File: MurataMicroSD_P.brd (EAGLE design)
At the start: 25.6 x 12.8 mm, 57 parts, among them U1 IC_BLE_LBCA2HNZYZ-711, U2 IC_BLE_LBCA2HNZYZ-711, U3 IC_BLE_LBCA2HNZYZ-711, U4 IC_BLE_LBCA2HNZYZ-711, U5 IC_BLE_LBCA2HNZYZ-711, U6 IC_BLE_LBCA2HNZYZ-711

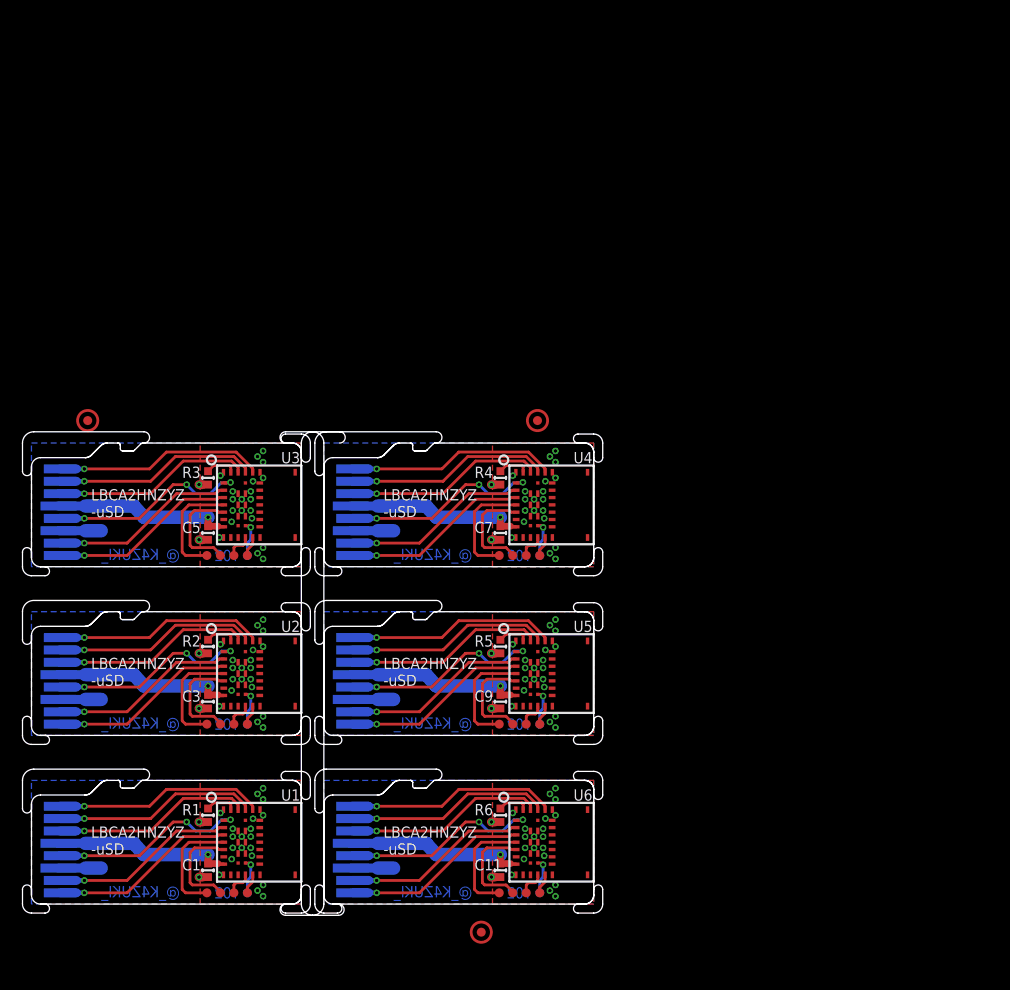
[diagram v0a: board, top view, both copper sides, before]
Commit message: [ uSD ] panelise as r3
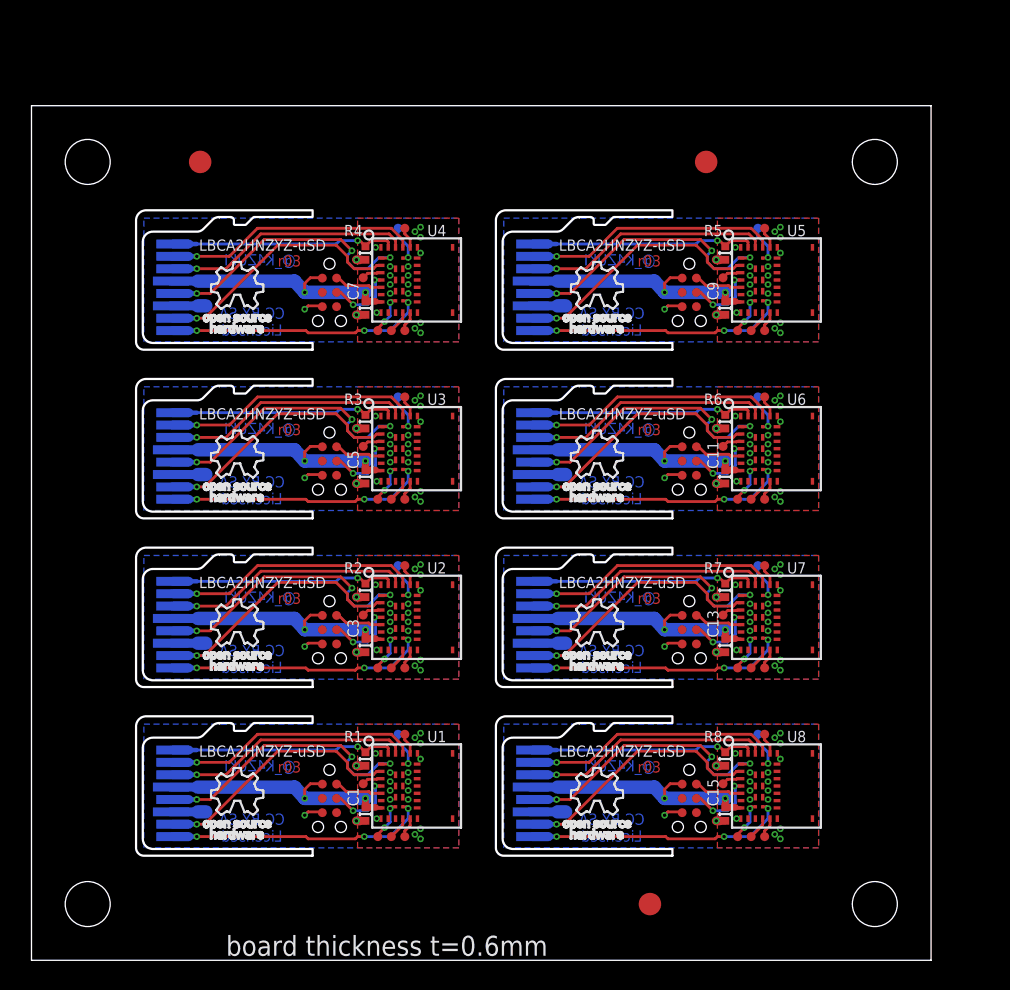
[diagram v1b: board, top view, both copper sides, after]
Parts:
- added C12, C14: BOARD_MICROSD, mylib:BOARD_MICROSD
- added C13, C15, R7, R8: (no value), mylib:C0402
- added CON1, CON2, CON3, CON4, CON5, CON6, CON7, CON8: CON_TC2030-CTL-NL, mylib:CON_TC2030-IDC-NL
- added TP34, TP35, TP36, TP37, TP38, TP39, TP40, TP41, TP42, TP43, TP44, TP45, TP46, TP47, TP48, TP49, TP50, TP51: TPTP08R, testpad_local:TP08R
- added U7, U8: IC_BLE_LBCA2HNZYZ-711, mylib:IC_MURATA_LBCA2HNZYZ-711
- TP3, TP4, TP5: value TPTP08R -> TPTP20R; device testpad_local:TP08R -> testpad_local:TP20R
- moved TP30 63.2 mm to (65.2, 65.1)
- moved TP31 62.2 mm to (64.6, 65.1)
- moved TP33 57.1 mm to (61.5, 60.7)
- moved TP29 55.3 mm to (65.2, 56.0)
- moved TP32 53.4 mm to (62.8, 56.0)
- moved TP25 45.3 mm to (32.6, 65.1), flipped to the bottom
- moved TP24 44.9 mm to (33.2, 65.1)
- moved TP27 42.3 mm to (29.5, 60.7)
- moved C11 40.3 mm to (61.7, 43.0)
- moved C9 40.3 mm to (61.7, 58.0)
- moved R5 40.3 mm to (61.7, 62.9)
- moved R6 40.3 mm to (61.7, 47.9)
- moved U5 40.3 mm to (62.5, 64.0)
- moved U6 40.3 mm to (62.5, 49.0)
- moved TP28 39.7 mm to (64.0, 56.0)
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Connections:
- removed net DAT10: C8.1_DAT2, U5.22
- removed net DAT11: C10.8_DAT1, U6.3
- removed net DAT12: C10.1_DAT2, U6.22
- removed net DAT9: C8.8_DAT1, U5.3
- new net !CS!6: C12.2_CS, U7.23
- new net !CS!7: C14.2_CS, U8.23
- new net 3.3V6: C12.4_VDD, C13.1, CON7.1, U7.7
- new net 3.3V7: C14.4_VDD, C15.1, CON8.1, U8.7
- new net GND6: C12.6_VSS, C13.2, CON7.5, R7.1, U7.15, U7.16, U7.17, U7.18, U7.20, U7.21, U7.26, U7.27, U7.28, U7.29, U7.32, U7.33, U7.34, U7.6, U7.8
- new net GND7: C14.6_VSS, C15.2, CON8.5, R8.1, U8.15, U8.16, U8.17, U8.18, U8.20, U8.21, U8.26, U8.27, U8.28, U8.29, U8.32, U8.33, U8.34, U8.6, U8.8
- new net MISO6: C12.7_MISO, U7.2
- new net MISO7: C14.7_MISO, U8.2
- new net N$13: C12.1_DAT2, R7.2, U7.25
- new net N$14: C12.8_DAT1, U7.31
- new net N$15: C14.1_DAT2, R8.2, U8.25
- new net N$16: C14.8_DAT1, U8.31
- new net P0_13: TP28.TP, U5.11
- new net P0_14: TP29.TP, U5.12
- new net P0_15: TP30.TP, U5.22
- new net P0_16: TP34.TP, U6.11
- new net P0_17: TP35.TP, U6.12
- new net P0_18: TP36.TP, U6.22
- new net P0_19: TP40.TP, U7.11
- new net P0_20: TP41.TP, U7.12
- new net P0_21: TP42.TP, U7.22
- new net P0_22: TP46.TP, U8.11
- new net P0_23: TP47.TP, U8.12
- new net P0_24: TP48.TP, U8.22
- new net P1_0: TP10.TP, U1.35
- new net P1_1: TP11.TP, U1.30
- new net P1_10: TP37.TP, U6.35
- new net P1_11: TP38.TP, U6.30
- new net P1_12: TP43.TP, U7.35
- new net P1_13: TP44.TP, U7.30
- new net P1_14: TP49.TP, U8.35
- new net P1_15: TP50.TP, U8.30
- new net P1_2: TP13.TP, U2.35
- new net P1_3: TP14.TP, U2.30
- new net P1_4: TP19.TP, U3.35
- new net P1_5: TP20.TP, U3.30
- new net P1_6: TP25.TP, U4.35
- new net P1_7: TP26.TP, U4.30
- new net P1_8: TP31.TP, U5.35
- new net P1_9: TP32.TP, U5.30
- new net RXD_MOSI6: C12.3_MOSI, U7.24
- new net RXD_MOSI7: C14.3_MOSI, U8.24
- new net SCK6: C12.5_CLK, U7.1
- new net SCK7: C14.5_CLK, U8.1
- new net SWCLK6: CON7.4, U7.4
- new net SWCLK7: CON8.4, U8.4
- new net SWDIO6: CON7.2, U7.5
- new net SWDIO7: CON8.2, U8.5
- net 3.3V: now also CON1.1
- net 3.3V1: now also CON2.1
- net 3.3V2: now also CON3.1
- net 3.3V3: now also CON4.1
- net 3.3V4: now also CON5.1
- net 3.3V5: now also CON6.1
- net DAT1: now also TP1.TP; no longer C100.8_DAT1
- net DAT2: now also TP15.TP, U2.3; no longer C100.1_DAT2, U1.22
- net DAT3: now also TP21.TP, U3.3; no longer C2.8_DAT1, U2.3
- net DAT4: now also TP27.TP, U4.3; no longer C2.1_DAT2, U2.22
- net DAT5: now also TP33.TP, U5.3; no longer C4.8_DAT1, U3.3
- net DAT6: now also TP39.TP, U6.3; no longer C4.1_DAT2, U3.22
- net DAT7: now also TP45.TP, U7.3; no longer C6.8_DAT1, U4.3
- net DAT8: now also TP51.TP, U8.3; no longer C6.1_DAT2, U4.22
- net GND: now also CON1.5
- net GND1: now also CON2.5
- net GND2: now also CON3.5
- net GND3: now also CON4.5
- net GND4: now also CON5.5
- net GND5: now also CON6.5
- net N$1: now also C100.1_DAT2
- net N$10: now also C8.8_DAT1; no longer TP26.TP
- net N$11: now also C10.1_DAT2
- net N$12: now also C10.8_DAT1; no longer TP31.TP
- net N$2: now also C100.8_DAT1; no longer TP6.TP
- net N$3: now also C2.1_DAT2
- net N$4: now also C2.8_DAT1; no longer TP11.TP
- net N$5: now also C4.1_DAT2
- net N$6: now also C4.8_DAT1; no longer TP16.TP
- net N$7: now also C6.1_DAT2
- net N$8: now also C6.8_DAT1; no longer TP21.TP
- net N$9: now also C8.1_DAT2
- net P0_1: now also TP9.TP, U1.22; no longer TP12.TP, U2.11
- net P0_10: now also TP22.TP, U4.11; no longer TP28.TP, U5.12
- net P0_11: now also TP23.TP, U4.12; no longer TP32.TP, U6.11
- net P0_12: now also TP24.TP, U4.22; no longer TP33.TP, U6.12
- net P0_4: now also TP2.TP, U2.11; no longer TP13.TP, U2.12
- net P0_5: now also TP6.TP, U2.12; no longer TP17.TP, U3.11
- net P0_6: now also TP12.TP, U2.22; no longer TP18.TP, U3.12
- net P0_7: now also TP16.TP, U3.11; no longer TP22.TP, U4.11
- net P0_8: now also TP17.TP, U3.12; no longer TP23.TP, U4.12
- net P0_9: now also TP18.TP, U3.22; no longer TP27.TP, U5.11
- net SWCLK: now also CON1.4; no longer TP1.TP
- net SWCLK1: now also CON2.4; no longer TP9.TP
- net SWCLK2: now also CON3.4; no longer TP14.TP
- net SWCLK3: now also CON4.4; no longer TP19.TP
- net SWCLK4: now also CON5.4; no longer TP24.TP
- net SWCLK5: now also CON6.4; no longer TP29.TP
- net SWDIO: now also CON1.2; no longer TP2.TP
- net SWDIO1: now also CON2.2; no longer TP10.TP
- net SWDIO2: now also CON3.2; no longer TP15.TP
- net SWDIO3: now also CON4.2; no longer TP20.TP
- net SWDIO4: now also CON5.2; no longer TP25.TP
- net SWDIO5: now also CON6.2; no longer TP30.TP
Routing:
- net SCK6: track 0.00 -> 24.8 mm, vias 0 -> 3
- net SCK7: track 0.00 -> 24.8 mm, vias 0 -> 3
- net N$16: track 0.00 -> 23.2 mm, vias 0 -> 3
- net N$14: track 0.00 -> 23.2 mm, vias 0 -> 3
- net !CS!7: track 0.00 -> 22.6 mm, vias 0 -> 1
- net !CS!6: track 0.00 -> 22.6 mm, vias 0 -> 1
- net 3.3V6: track 0.00 -> 22.6 mm, vias 0 -> 2
- net 3.3V7: track 0.00 -> 22.6 mm, vias 0 -> 2
- net MISO7: track 0.00 -> 22.5 mm, vias 0 -> 1
- net MISO6: track 0.00 -> 22.5 mm, vias 0 -> 1
- net RXD_MOSI7: track 0.00 -> 22.0 mm, vias 0 -> 1
- net RXD_MOSI6: track 0.00 -> 22.0 mm, vias 0 -> 1
- net N$15: track 0.00 -> 20.2 mm, vias 0 -> 1
- net N$13: track 0.00 -> 20.2 mm, vias 0 -> 1
- net N$8: track 3.16 -> 23.2 mm, vias 1 -> 3
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- added copper zone on layer 1, net GND6
- added copper zone on layer 16, net GND6
- added copper zone on layer 1, net GND7
- added copper zone on layer 16, net GND7
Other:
- board size 25.6 x 12.8 mm -> 80 x 76 mm
- board text added: "CC-BY-SA Licensed"
- board text added: "LBCA2HNZYZ-uSD"
- board text added: "board thickness t=0.6mm"
- board text added: "r03"
- board text removed: "LBCA2HNZYZ -uSD"
- board text removed: "r02"

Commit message: [ uSD ] panelised as r3
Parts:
- removed CON7, CON8: CON_TC2030-CTL-NL, mylib:CON_TC2030-IDC-NL
- removed R7, R8: (no value), mylib:C0402
- removed TP37, TP38, TP39, TP40, TP41, TP42, TP43, TP44, TP45, TP46, TP47, TP48, TP49, TP50, TP51: TPTP08R, testpad_local:TP08R
- removed U7, U8: IC_BLE_LBCA2HNZYZ-711, mylib:IC_MURATA_LBCA2HNZYZ-711
- added C16, C17: (no value), mylib:C0402
- added IC1, IC2, IC3, IC4, IC5, IC6: 1265-1139-1-ND, mylib:IC_08_0.65_160MIL
- added TP100, TP101, TP102: TPTP20R, testpad_local:TP20R
- added U$1, U$2, U$3, U$4, U$5, U$6: ICON_OSHW, mylib:ICON_OSHW
- C10, C14, C2, C4, C8: value BOARD_MICROSD -> (none); device mylib:BOARD_MICROSD -> mylib:C0402
- C15, C3, C9: value (none) -> BOARD_MICROSD; device mylib:C0402 -> mylib:BOARD_MICROSD
- TP3, TP4, TP5: value TPTP20R -> TPTP08R; device testpad_local:TP20R -> testpad_local:TP08R
- moved TP4 49.1 mm to (34.7, 49.7)
- moved TP21 48.7 mm to (70.2, 72.5)
- moved TP31 47.5 mm to (69.0, 17.8), flipped to the top
- moved TP20 45.3 mm to (70.2, 63.4)
- moved TP25 43.9 mm to (69.0, 40.6), flipped to the top
- moved TP26 42.3 mm to (70.2, 40.6)
- moved TP27 42.2 mm to (70.2, 49.7)
- moved TP15 42.1 mm to (34.7, 72.5)
- moved TP22 41.1 mm to (69.6, 72.5), flipped to the bottom
- moved CON4 39.2 mm to (65.7, 58.9), turned to 0 degrees
- moved TP32 38.9 mm to (70.2, 17.8)
- moved TP19 38.8 mm to (69.0, 63.4), flipped to the top
- moved R4 37.7 mm to (66.7, 70.3)
- moved U4 37.7 mm to (67.5, 71.4)
- moved TP14 37.6 mm to (34.7, 63.4)
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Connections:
- net N$2 renamed VPP
- removed net !CS!6: C12.2_CS, U7.23
- removed net !CS!7: C14.2_CS, U8.23
- removed net 3.3V6: C12.4_VDD, C13.1, CON7.1, U7.7
- removed net 3.3V7: C14.4_VDD, C15.1, CON8.1, U8.7
- removed net DAT1: TP1.TP, U1.3
- removed net DAT2: TP15.TP, U2.3
- removed net DAT3: TP21.TP, U3.3
- removed net DAT4: TP27.TP, U4.3
- removed net DAT5: TP33.TP, U5.3
- removed net DAT6: TP39.TP, U6.3
- removed net DAT7: TP45.TP, U7.3
- removed net DAT8: TP51.TP, U8.3
- removed net GND6: C12.6_VSS, C13.2, CON7.5, R7.1, U7.15, U7.16, U7.17, U7.18, U7.20, U7.21, U7.26, U7.27, U7.28, U7.29, U7.32, U7.33, U7.34, U7.6, U7.8
- removed net GND7: C14.6_VSS, C15.2, CON8.5, R8.1, U8.15, U8.16, U8.17, U8.18, U8.20, U8.21, U8.26, U8.27, U8.28, U8.29, U8.32, U8.33, U8.34, U8.6, U8.8
- removed net MISO6: C12.7_MISO, U7.2
- removed net MISO7: C14.7_MISO, U8.2
- removed net N$10: C8.8_DAT1, U5.31
- removed net N$11: C10.1_DAT2, R6.2, U6.25
- removed net N$12: C10.8_DAT1, U6.31
- removed net N$13: C12.1_DAT2, R7.2, U7.25
- removed net N$14: C12.8_DAT1, U7.31
- removed net N$15: C14.1_DAT2, R8.2, U8.25
- removed net N$16: C14.8_DAT1, U8.31
- removed net N$7: C6.1_DAT2, R4.2, U4.25
- removed net N$8: C6.8_DAT1, U4.31
- removed net N$9: C8.1_DAT2, R5.2, U5.25
- removed net P1_12: TP43.TP, U7.35
- removed net P1_13: TP44.TP, U7.30
- removed net P1_14: TP49.TP, U8.35
- removed net P1_15: TP50.TP, U8.30
- removed net RXD_MOSI6: C12.3_MOSI, U7.24
- removed net RXD_MOSI7: C14.3_MOSI, U8.24
- removed net SCK6: C12.5_CLK, U7.1
- removed net SCK7: C14.5_CLK, U8.1
- removed net SWCLK6: CON7.4, U7.4
- removed net SWCLK7: CON8.4, U8.4
- removed net SWDIO6: CON7.2, U7.5
- removed net SWDIO7: CON8.2, U8.5
- new net N$2: C3.1_DAT2, R2.2, U2.25
- new net VPP1: C3.8_DAT1, U2.31
- new net VPP2: C6.8_DAT1, U3.31
- new net VPP3: C9.8_DAT1, U4.31
- new net VPP4: C12.8_DAT1, U5.31
- new net VPP5: C15.8_DAT1, U6.31
- net !CS!: now also IC1.1
- net !CS!1: now also C3.2_CS, IC2.1; no longer C2.2_CS
- net !CS!2: now also C6.2_CS, IC3.1; no longer C4.2_CS
- net !CS!3: now also C9.2_CS, IC4.1; no longer C6.2_CS
- net !CS!4: now also C12.2_CS, IC5.1; no longer C8.2_CS
- net !CS!5: now also C15.2_CS, IC6.1; no longer C10.2_CS
- net 3.3V: now also C2.1, IC1.3, IC1.7, IC1.8
- net 3.3V1: now also C3.4_VDD, C4.1, C5.1, IC2.3, IC2.7, IC2.8; no longer C2.4_VDD, C3.1
- net 3.3V2: now also C6.4_VDD, C7.1, C8.1, IC3.3, IC3.7, IC3.8; no longer C4.4_VDD, C5.1
- net 3.3V3: now also C10.1, C11.1, C9.4_VDD, IC4.3, IC4.7, IC4.8; no longer C6.4_VDD, C7.1
- net 3.3V4: now also C12.4_VDD, C13.1, C14.1, IC5.3, IC5.7, IC5.8; no longer C8.4_VDD, C9.1
- net 3.3V5: now also C15.4_VDD, C16.1, C17.1, IC6.3, IC6.7, IC6.8; no longer C10.4_VDD, C11.1
- net GND: now also C2.2, IC1.4
- net GND1: now also C3.6_VSS, C4.2, C5.2, IC2.4; no longer C2.6_VSS, C3.2
- net GND2: now also C6.6_VSS, C7.2, C8.2, IC3.4; no longer C4.6_VSS, C5.2
- net GND3: now also C10.2, C11.2, C9.6_VSS, IC4.4; no longer C6.6_VSS, C7.2
- net GND4: now also C12.6_VSS, C13.2, C14.2, IC5.4; no longer C8.6_VSS, C9.2
- net GND5: now also C15.6_VSS, C16.2, C17.2, IC6.4; no longer C10.6_VSS, C11.2
- net MISO: now also IC1.2
- net MISO1: now also C3.7_MISO, IC2.2; no longer C2.7_MISO
- net MISO2: now also C6.7_MISO, IC3.2; no longer C4.7_MISO
- net MISO3: now also C9.7_MISO, IC4.2; no longer C6.7_MISO
- net MISO4: now also C12.7_MISO, IC5.2; no longer C8.7_MISO
- net MISO5: now also C15.7_MISO, IC6.2; no longer C10.7_MISO
- net N$3: now also C6.1_DAT2, R3.2, U3.25; no longer C2.1_DAT2, R2.2, U2.25
- net N$4: now also C9.1_DAT2, R4.2, U4.25; no longer C2.8_DAT1, U2.31
- net N$5: now also C12.1_DAT2, R5.2, U5.25; no longer C4.1_DAT2, R3.2, U3.25
- net N$6: now also C15.1_DAT2, R6.2, U6.25; no longer C4.8_DAT1, U3.31
- net P0_10: now also TP13.TP, U3.11; no longer TP22.TP, U4.11
- net P0_11: now also TP14.TP, U3.12; no longer TP23.TP, U4.12
- net P0_12: now also TP15.TP, U3.22; no longer TP24.TP, U4.22
- net P0_13: now also TP24.TP, U4.3; no longer TP28.TP, U5.11
- net P0_14: now also TP19.TP, U4.11; no longer TP29.TP, U5.12
- net P0_15: now also TP20.TP, U4.12; no longer TP30.TP, U5.22
- net P0_16: now also TP21.TP, U4.22; no longer TP34.TP, U6.11
- net P0_17: now also TP30.TP, U5.3; no longer TP35.TP, U6.12
- net P0_18: now also TP25.TP, U5.11; no longer TP36.TP, U6.22
- net P0_19: now also TP26.TP, U5.12; no longer TP40.TP, U7.11
- net P0_20: now also TP27.TP, U5.22; no longer TP41.TP, U7.12
- net P0_21: now also TP36.TP, U6.3; no longer TP42.TP, U7.22
- net P0_22: now also TP31.TP, U6.11; no longer TP46.TP, U8.11
- net P0_23: now also TP32.TP, U6.12; no longer TP47.TP, U8.12
- net P0_24: now also TP33.TP, U6.22; no longer TP48.TP, U8.22
- net P0_4: now also TP12.TP, U2.3; no longer TP2.TP, U2.11
- net P0_5: now also TP2.TP, U2.11; no longer TP6.TP, U2.12
- net P0_6: now also TP1.TP, U1.3; no longer TP12.TP, U2.22
- net P0_7: now also TP3.TP, U2.12; no longer TP16.TP, U3.11
- net P0_8: now also TP4.TP, U2.22; no longer TP17.TP, U3.12
- net P0_9: now also U3.3; no longer U3.22
- net P1_10: now also TP34.TP; no longer TP37.TP
- net P1_11: now also TP35.TP; no longer TP38.TP
- net P1_2: now also TP5.TP; no longer TP13.TP
- net P1_3: now also TP6.TP; no longer TP14.TP
- net P1_4: now also TP16.TP; no longer TP19.TP
- net P1_5: now also TP17.TP; no longer TP20.TP
- net P1_6: now also TP22.TP; no longer TP25.TP
- net P1_7: now also TP23.TP; no longer TP26.TP
- net P1_8: now also TP28.TP; no longer TP31.TP
- net P1_9: now also TP29.TP; no longer TP32.TP
- net RXD_MOSI: now also IC1.5
- net RXD_MOSI1: now also C3.3_MOSI, IC2.5; no longer C2.3_MOSI
- net RXD_MOSI2: now also C6.3_MOSI, IC3.5; no longer C4.3_MOSI
- net RXD_MOSI3: now also C9.3_MOSI, IC4.5; no longer C6.3_MOSI
- net RXD_MOSI4: now also C12.3_MOSI, IC5.5; no longer C8.3_MOSI
- net RXD_MOSI5: now also C15.3_MOSI, IC6.5; no longer C10.3_MOSI
- net SCK: now also IC1.6
- net SCK1: now also C3.5_CLK, IC2.6; no longer C2.5_CLK
- net SCK2: now also C6.5_CLK, IC3.6; no longer C4.5_CLK
- net SCK3: now also C9.5_CLK, IC4.6; no longer C6.5_CLK
- net SCK4: now also C12.5_CLK, IC5.6; no longer C8.5_CLK
- net SCK5: now also C15.5_CLK, IC6.6; no longer C10.5_CLK
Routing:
- net SCK6: track 24.8 -> 0.00 mm, vias 3 -> 0
- net SCK7: track 24.8 -> 0.00 mm, vias 3 -> 0
- net VPP4: track 0.00 -> 24.7 mm, vias 0 -> 1
- net VPP1: track 0.00 -> 24.7 mm, vias 0 -> 1
- net VPP5: track 0.00 -> 24.7 mm, vias 0 -> 1
- net VPP2: track 0.00 -> 24.7 mm, vias 0 -> 1
- net VPP3: track 0.00 -> 24.7 mm, vias 0 -> 1
- net N$8: track 23.2 -> 0.00 mm, vias 3 -> 0
- net N$16: track 23.2 -> 0.00 mm, vias 3 -> 0
- net N$14: track 23.2 -> 0.00 mm, vias 3 -> 0
- net N$12: track 23.2 -> 0.00 mm, vias 3 -> 0
- net N$10: track 23.2 -> 0.00 mm, vias 3 -> 0
- net !CS!7: track 22.6 -> 0.00 mm, vias 1 -> 0
- net !CS!6: track 22.6 -> 0.00 mm, vias 1 -> 0
- net 3.3V6: track 22.6 -> 0.00 mm, vias 2 -> 0
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- removed copper zone on layer 1, net GND6
- removed copper zone on layer 16, net GND6
- removed copper zone on layer 1, net GND7
- removed copper zone on layer 16, net GND7
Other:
- board size 80 x 76 mm -> 85 x 83.4 mm
- board text added: "C2"
- board text added: "IC1"
